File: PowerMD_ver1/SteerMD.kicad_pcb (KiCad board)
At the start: 2 copper layers, 75 x 88 mm, 216 parts, among them P1 SWD, P10 OUT_1, P11 ENC_0, P13 ENC_1, P14 I/O_1, P15 OUT_0, P2 MOTOR_COOLING, P3 CAN, P4 CAN, P5 SERIAL, P6 I/O_0, P7 FAN, P8 BATT_IN, P9 BATT_IN, Q1 MOSFET_N, Q2 MOSFET_N, Q3 MOSFET_N, Q4 MOSFET_N, Q5 MOSFET_N, Q6 MOSFET_N, Q7 MOSFET_N, Q8 MOSFET_N, SW1 RST, SW3 SW0, SW4 SW1, U1 MAX3051, U10 ACS758, U11 POWER_ON, U12 SI8274, U13 ACS758, U14 SI8274, U15 AZ1086H, U16 LOGO, U17 AQM0802, U19 ADRESS, U2 BD9G101, U3 STM32F405RG, U4 SI8274, U5 SI8900, U6 ADC_~RST, U7 BD9G101G, U8 SI8274, U9 BD33FA1, Y1 8MHz

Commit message: ハイサイド電流センシングバージョンとローサイド電流センシングバージョン
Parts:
- moved C34 0.55 mm to (82.2, 83.4)
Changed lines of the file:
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@@
   )
   (setup
-    (last_trace_width 0.25)
+    (last_trace_width 0.2)
     (user_trace_width 0.2)
     (user_trace_width 0.3)
@@
   )
   (module Mizz_lib:C_Radial_D13.0mm_H25.0mm_P5.00mm (layer F.Cu)
-    (at 82.25 83.975 180)
+    (at 82.22 83.43 180)
     (descr "C, Radial series, Radial, pin pitch=5.00mm, diameter=12.5mm, height=25mm, Non-Polar Electrolytic Capacitor")
     (tags "C Radial series Radial pin pitch 5.00mm diameter 12.5mm height 25mm Non-Polar Electrolytic Capacitor")
@@
   (via (at 110.87 118.57) (size 0.5) (drill 0.3) (layers F.Cu B.Cu) (net 2))
   (via (at 103.6 117.3) (size 0.8) (drill 0.4) (layers F.Cu B.Cu) (net 2))
-  (via (at 96.45 110) (size 0.5) (drill 0.3) (layers F.Cu B.Cu) (net 2))
   (via (at 102.35 110) (size 0.5) (drill 0.3) (layers F.Cu B.Cu) (net 2))
   (via (at 101.6 108.35) (size 0.5) (drill 0.3) (layers F.Cu B.Cu) (net 2))
@@
   (via (at 120.95 123.3) (size 0.5) (drill 0.3) (layers F.Cu B.Cu) (net 2))
   (via (at 79.05 113.15) (size 0.8) (drill 0.4) (layers F.Cu B.Cu) (net 2))
+  (via (at 96.45 110) (size 0.5) (drill 0.3) (layers F.Cu B.Cu) (net 2) (status 1000000))
   (segment (start 139.95 129.3375) (end 140.5125 129.9) (width 0.25) (layer B.Cu) (net 3))
   (segment (start 139.95 126.7) (end 139.95 129.3375) (width 0.25) (layer B.Cu) (net 3))
@@
   (segment (start 112.746179 113.653159) (end 112.687979 113.653159) (width 0.2) (layer F.Cu) (net 69))
   (segment (start 112.687979 113.653159) (end 111.864589 112.829769) (width 0.2) (layer F.Cu) (net 69))
+  (segment (start 106.80001 109.40001) (end 110.775001 113.375001) (width 0.25) (layer B.Cu) (net 69))
   (segment (start 90.68 112.2) (end 92.3 112.2) (width 0.25) (layer B.Cu) (net 69))
-  (segment (start 111.319357 113.375001) (end 111.864589 112.829769) (width 0.25) (layer B.Cu) (net 69))
   (segment (start 90.225 112.655) (end 90.68 112.2) (width 0.25) (layer B.Cu) (net 69))
-  (segment (start 92.3 112.2) (end 95.09999 109.40001) (width 0.25) (layer B.Cu) (net 69))
   (segment (start 95.09999 109.40001) (end 106.80001 109.40001) (width 0.25) (layer B.Cu) (net 69))
-  (segment (start 106.80001 109.40001) (end 110.775001 113.375001) (width 0.25) (layer B.Cu) (net 69))
+  (segment (start 111.319357 113.375001) (end 111.864589 112.829769) (width 0.25) (layer B.Cu) (net 69))
+  (segment (start 92.3 112.2) (end 95.09999 109.40001) (width 0.25) (layer B.Cu) (net 69))
   (segment (start 110.775001 113.375001) (end 111.319357 113.375001) (width 0.25) (layer B.Cu) (net 69))
   (via (at 111.05 112.8) (size 0.5) (drill 0.3) (layers F.Cu B.Cu) (net 70))
@@
   (segment (start 108.174999 109.924999) (end 111.05 112.8) (width 0.25) (layer B.Cu) (net 70))
   (segment (start 107.2 108.95) (end 108.174999 109.924999) (width 0.25) (layer B.Cu) (net 70))
-  (segment (start 90.685 108.845) (end 91.296494 109.456494) (width 0.25) (layer B.Cu) (net 70))
+  (segment (start 90.685 108.845) (end 91.296494 109.456494) (width 0.25) (layer B.Cu) (net 70) (status 1000000))
+  (segment (start 93.93858 109.92501) (end 94.91359 108.95) (width 0.25) (layer B.Cu) (net 70) (status 1000000))
+  (segment (start 90.225 108.845) (end 90.685 108.845) (width 0.25) (layer B.Cu) (net 70) (status 1000000))
+  (segment (start 91.3 109.456494) (end 91.768516 109.92501) (width 0.25) (layer B.Cu) (net 70) (status 1000000))
+  (segment (start 91.296494 109.456494) (end 91.3 109.456494) (width 0.25) (layer B.Cu) (net 70) (status 1000000))
+  (segment (start 91.768516 109.92501) (end 93.93858 109.92501) (width 0.25) (layer B.Cu) (net 70) (status 1000000))
   (segment (start 94.91359 108.95) (end 107.2 108.95) (width 0.25) (layer B.Cu) (net 70))
-  (segment (start 91.3 109.456494) (end 91.768516 109.92501) (width 0.25) (layer B.Cu) (net 70))
-  (segment (start 91.296494 109.456494) (end 91.3 109.456494) (width 0.25) (layer B.Cu) (net 70))
-  (segment (start 91.768516 109.92501) (end 93.93858 109.92501) (width 0.25) (layer B.Cu) (net 70))
-  (segment (start 90.225 108.845) (end 90.685 108.845) (width 0.25) (layer B.Cu) (net 70))
-  (segment (start 93.93858 109.92501) (end 94.91359 108.95) (width 0.25) (layer B.Cu) (net 70))
   (segment (start 140.885 105.725) (end 140.885 104.6) (width 0.2) (layer F.Cu) (net 71))
   (segment (start 121.832501 111.527499) (end 123.89 109.47) (width 0.2) (layer F.Cu) (net 71))
@@
   (segment (start 109.1 107.4) (end 105.95501 110.54499) (width 0.2) (layer F.Cu) (net 109))
   (segment (start 105.95501 110.54499) (end 94.95501 110.54499) (width 0.2) (layer F.Cu) (net 109))
-  (segment (start 112.59 107.4) (end 109.1 107.4) (width 0.2) (layer F.Cu) (net 109))
   (segment (start 94.95501 110.54499) (end 94.35001 111.14999) (width 0.2) (layer F.Cu) (net 109))
   (segment (start 94.35001 111.14999) (end 94.35001 118.55001) (width 0.2) (layer F.Cu) (net 109))
   (segment (start 94.35001 118.55001) (end 94.599989 118.799989) (width 0.2) (layer F.Cu) (net 109))
-  (segment (start 97.412501 119.199999) (end 97.9625 118.65) (width 0.2) (layer F.Cu) (net 110))
-  (segment (start 94.299999 119.199999) (end 97.412501 119.199999) (width 0.2) (layer F.Cu) (net 110))
-  (segment (start 93.95 118.85) (end 94.299999 119.199999) (width 0.2) (layer F.Cu) (net 110))
-  (segment (start 93.95 110.95) (end 93.95 118.85) (width 0.2) (layer F.Cu) (net 110))
-  (segment (start 94.9 110) (end 93.95 110.95) (width 0.2) (layer F.Cu) (net 110))
-  (segment (start 94.9 110) (end 95.6 110) (width 0.2) (layer F.Cu) (net 110))
-  (segment (start 95.6 110) (end 97.1 108.5) (width 0.2) (layer F.Cu) (net 110))
-  (segment (start 97.1 108.5) (end 97.1 106.6) (width 0.2) (layer F.Cu) (net 110))
+  (segment (start 112.59 107.4) (end 109.1 107.4) (width 0.2) (layer F.Cu) (net 109))
   (segment (start 96.595 106.095) (end 97.1 106.6) (width 0.2) (layer F.Cu) (net 110))
+  (segment (start 93.95 110.95) (end 93.95 118.85) (width 0.2) (layer F.Cu) (net 110))
   (segment (start 93.395 106.095) (end 96.595 106.095) (width 0.2) (layer F.Cu) (net 110))
   (segment (start 92.09 107.4) (end 93.395 106.095) (width 0.2) (layer F.Cu) (net 110))
+  (segment (start 95.6 110) (end 97.1 108.5) (width 0.2) (layer F.Cu) (net 110))
+  (segment (start 94.9 110) (end 95.6 110) (width 0.2) (layer F.Cu) (net 110))
+  (segment (start 97.1 108.5) (end 97.1 106.6) (width 0.2) (layer F.Cu) (net 110))
+  (segment (start 94.9 110) (end 93.95 110.95) (width 0.2) (layer F.Cu) (net 110))
+  (segment (start 97.412501 119.199999) (end 97.9625 118.65) (width 0.2) (layer F.Cu) (net 110))
+  (segment (start 93.95 118.85) (end 94.299999 119.199999) (width 0.2) (layer F.Cu) (net 110))
+  (segment (start 94.299999 119.199999) (end 97.412501 119.199999) (width 0.2) (layer F.Cu) (net 110))
   (segment (start 111.005 95.18) (end 110.9 95.075) (width 0.5) (layer F.Cu) (net 119))
   (segment (start 111.005 97.675) (end 111.005 95.18) (width 0.5) (layer F.Cu) (net 119))

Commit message: 途中
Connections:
- C20 pad 2: GNDPWR -> /MOTOR0_BATT
- C31 pad 2: GNDPWR -> /MOTOR0_BATT
- C46 pad 2: GNDPWR -> /MOTOR1_BATT
- C49 pad 2: GNDPWR -> /MOTOR1_BATT
- Q1 pad D: /MOTOR0_BATT -> +BATT
- Q2 pad S: GNDPWR -> /MOTOR0_BATT
- Q3 pad D: /MOTOR1_BATT -> +BATT
- Q4 pad S: GNDPWR -> /MOTOR1_BATT
- Q5 pad D: /MOTOR0_BATT -> +BATT
- Q6 pad S: GNDPWR -> /MOTOR0_BATT
- Q7 pad D: /MOTOR1_BATT -> +BATT
- Q8 pad S: GNDPWR -> /MOTOR1_BATT
- U10 pad 4: +BATT -> /MOTOR0_BATT
- U10 pad 5: /MOTOR0_BATT -> GNDPWR
- U12 pad 9: GNDPWR -> /MOTOR0_BATT
- U13 pad 4: +BATT -> /MOTOR1_BATT
- U13 pad 5: /MOTOR1_BATT -> GNDPWR
- U14 pad 9: GNDPWR -> /MOTOR1_BATT
- U4 pad 9: GNDPWR -> /MOTOR0_BATT
- U8 pad 9: GNDPWR -> /MOTOR1_BATT
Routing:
- net GNDPWR: track 77.2 -> 66.6 mm, vias 36 -> 32
- net /MOTOR1_BATT: track 0.00 -> 5.31 mm, vias 38 -> 2
- net +BATT: track 104.8 -> 108.9 mm
- net /MOTOR0_BATT: track 4.09 -> 5.31 mm, vias 35 -> 2
- net +12P: track 89.4 -> 89.9 mm
- removed copper zone on B.Cu, net +BATT
- removed copper zone on F.Cu, net /MOTOR0_BATT
- removed copper zone on F.Cu, net /MOTOR1_BATT
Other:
- board text added: "CAN DC-MotroDriver Aqualius Sadalmeric ver.1.0"
- board text removed: "CAN DC-MotroDriver Aqualius Sadalmeric ver.0.0"

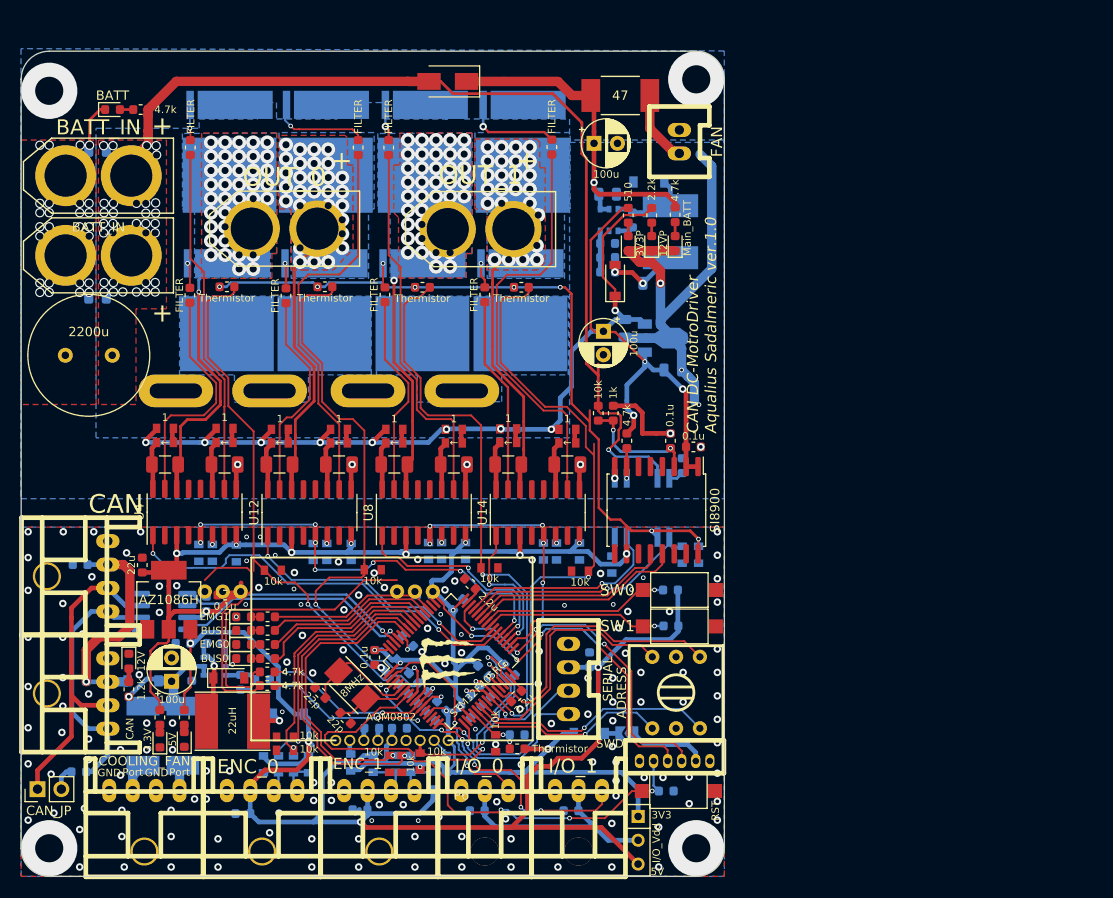
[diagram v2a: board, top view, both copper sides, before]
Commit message: Power MD 電流センシングをローサイドでセンシングするように変更した&DAC乗っけた
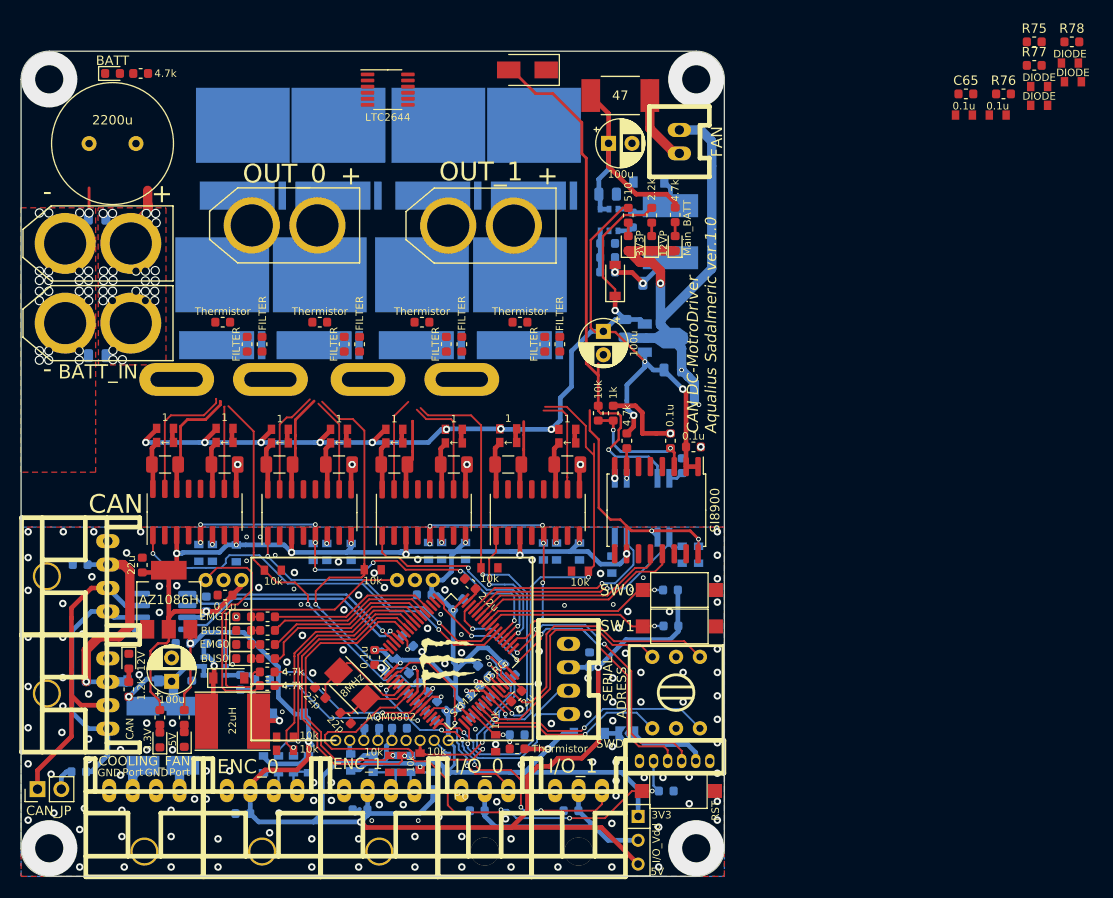
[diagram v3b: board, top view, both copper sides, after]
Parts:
- added C27: 0.1u, Mizz_lib:1608_WP, F.Cu at (173.1, 57.8)
- added C51: 0.1u, Mizz_lib:1608_WP, F.Cu at (176.7, 57.8)
- added C65: 0.1u, Capacitor_SMD:C_0603_1608Metric, F.Cu at (173.3, 55.6)
- added D10: DIODE, Mizz_lib:1608_WP, F.Cu at (184.3, 52.3)
- added D12: DIODE, Mizz_lib:1608_WP, F.Cu at (181.1, 56.8)
- added D17: DIODE, Mizz_lib:1608_WP, F.Cu at (184.7, 54.3)
- added D6: DIODE, Mizz_lib:1608_WP, F.Cu at (181.1, 54.8)
- added R75: 10k, Resistor_SMD:R_0603_1608Metric, F.Cu at (180.5, 50.0)
- added R76: 1k, Resistor_SMD:R_0603_1608Metric, F.Cu at (177.3, 55.6)
- added R77: 10k, Resistor_SMD:R_0603_1608Metric, F.Cu at (180.5, 52.5)
- added R78: 1k, Resistor_SMD:R_0603_1608Metric, F.Cu at (184.6, 50.0)
- added U18: LTC2644, Package_SO:MSOP-12_3x4mm_P0.65mm, F.Cu at (111.6, 55.1)
- moved C34 22.7 mm to (84.8, 60.9)
- moved R54 22.4 mm to (119.5, 82.2)
- moved R18 22.3 mm to (98.2, 82.2)
- moved R64 21.0 mm to (129.9, 82.2)
- moved R31 21.0 mm to (108.6, 82.2)
- moved Q1 17.3 mm to (96.2, 61.4), turned to 180 degrees
- moved Q3 17.3 mm to (117.0, 61.4), turned to 180 degrees
- moved Q5 17.3 mm to (106.3, 61.4), turned to 180 degrees
- moved Q7 17.3 mm to (127.2, 61.4), turned to 180 degrees
- moved Q2 15.6 mm to (94.0, 77.3), turned to 180 degrees
- moved Q6 15.6 mm to (104.3, 77.3), turned to 180 degrees
- moved Q4 15.6 mm to (115.2, 77.3), turned to 180 degrees
- moved Q8 15.6 mm to (125.7, 77.3), turned to 180 degrees
- moved D15 8.59 mm to (126.5, 53.0)
- moved R53 8.41 mm to (117.8, 82.2)
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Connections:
- U5 pad 4: /CounterVoltage0 -> /MOTOR0_VOLTAGE_DAC
- U5 pad 5: /CounterVoltage1 -> /MOTOR1_VOLTAGE_DAC
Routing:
- net +3V3: track 289.3 -> 236.2 mm, vias 25 -> 20
- net +BATT: track 108.9 -> 65.0 mm, vias 34 -> 27
- net Net-(R64-Pad2): track 44.4 -> 10.6 mm
- net Net-(R31-Pad2): track 42.0 -> 10.0 mm
- net Net-(R54-Pad2): track 40.0 -> 11.6 mm
- net Net-(R18-Pad2): track 37.1 -> 8.79 mm
- net /OUT1_R: track 30.2 -> 7.39 mm, vias 25 -> 0
- net Net-(R63-Pad2): track 20.9 -> 0.00 mm
- net /OUT0_R: track 30.8 -> 10.4 mm, vias 29 -> 0
- net /OUT1_L: track 27.7 -> 7.50 mm, vias 38 -> 0
- net /OUT0_L: track 31.4 -> 13.9 mm, vias 38 -> 0
- net /Motor1R_Tmp: track 69.8 -> 52.6 mm
- net /Motor0L_Tmp: track 62.6 -> 45.5 mm
- net /Motor0R_Tmp: track 63.2 -> 47.3 mm
- net /Motor1L_Tmp: track 65.8 -> 50.5 mm
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- removed copper zone on B.Cu, net /MOTOR0_BATT
- removed copper zone on B.Cu, net /MOTOR1_BATT
- removed copper zone on B.Cu, net /OUT0_L
- removed copper zone on F.Cu, net /OUT0_L
- removed copper zone on B.Cu, net /OUT0_R
- removed copper zone on F.Cu, net /OUT0_R
- removed copper zone on B.Cu, net /OUT1_L
- removed copper zone on F.Cu, net /OUT1_L
- removed copper zone on B.Cu, net /OUT1_R
- removed copper zone on F.Cu, net /OUT1_R
- removed copper zone on B.Cu, net GNDPWR
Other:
- board text added: "-"

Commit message: ブラシレス復元の続き
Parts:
- R17, R18, R30, R31, R53, R54, R63, R64: footprint Resistor_SMD:R_0603_1608Metric -> Mizz_lib:1608_WP
- TH1, TH2, TH3, TH4: footprint Capacitor_SMD:C_0603_1608Metric -> Mizz_lib:1608_WP
- moved TH1 0.65 mm to (93.3, 79.9)
- moved TH4 0.60 mm to (125.1, 79.9)
- moved TH2 0.60 mm to (114.7, 79.9)
- moved TH3 0.60 mm to (103.8, 79.9)

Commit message: だいぶ良いところまで進んだ
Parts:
- added C66: 0.1u, Mizz_lib:1608_WP, F.Cu at (115.3, 58.5)
- added C67: 0.1u, Mizz_lib:1608_WP, F.Cu at (107.0, 58.5)
- C65: footprint Capacitor_SMD:C_0603_1608Metric -> Mizz_lib:1608_WP
- D1, D10, D11, D12, D13, D14, D17, D19, D2, D20, D3, D6: footprint Mizz_lib:1608_WP -> Diode_SMD:D_SOD-123
- R19, R20, R28, R29, R55, R56, R58, R59: value 1 -> 10
- R40: value 4.7k -> 20k
- R75, R76, R77, R78: footprint Resistor_SMD:R_0603_1608Metric -> Mizz_lib:1608_WP
- moved D17 81.9 mm to (102.8, 55.9), turned to 180 degrees
- moved R78 79.2 mm to (105.8, 58.5), turned to 270 degrees
- moved D12 78.4 mm to (102.8, 53.6), turned to 180 degrees
- moved R77 76.4 mm to (104.4, 58.5), turned to 90 degrees
- moved D10 66.2 mm to (118.2, 53.7)
- moved C27 64.7 mm to (108.5, 60.5), turned to 180 degrees
- moved C51 64.4 mm to (112.3, 60.5)
- moved R75 64.4 mm to (116.8, 58.5), turned to 90 degrees
- moved R76 63.4 mm to (114.0, 58.5), turned to 270 degrees
- moved D6 62.9 mm to (118.2, 56.0)
- moved C65 59.3 mm to (114.0, 55.4), turned to 90 degrees
- moved P15 1.86 mm to (99.5, 68.1)
- moved U18 1.71 mm to (111.0, 56.7), turned to 90 degrees
- moved P10 1.70 mm to (120.8, 68.1)
- moved Q1 1.51 mm to (95.3, 60.1)
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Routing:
- net +12P: track 89.9 -> 21.8 mm, vias 9 -> 1
- net /MOTOR0_VOLTAGE_DAC: track 0.00 -> 63.7 mm, vias 0 -> 2
- net /MOTOR1_VOLTAGE_DAC: track 0.00 -> 62.4 mm, vias 0 -> 2
- net +BATT: track 65.0 -> 118.3 mm, vias 27 -> 26
- net GNDPWR: track 69.3 -> 86.2 mm, vias 30 -> 29
- net +3.3VP: track 47.5 -> 63.5 mm
- net /OUT1_R: track 7.39 -> 18.9 mm, vias 0 -> 1
- net /MOTOR0_OUT: track 0.00 -> 11.1 mm
- net /MOTOR1_OUT: track 0.00 -> 10.8 mm
- net /OUT0_L: track 13.9 -> 4.20 mm
- net /Motor1R_Tmp: track 52.6 -> 43.9 mm
- net /OUT0_R: track 10.4 -> 2.64 mm
- net /OUT1_L: track 7.50 -> 14.7 mm, vias 0 -> 1
- net Net-(D10-Pad1): track 0.00 -> 6.73 mm
- net Net-(D12-Pad1): track 0.00 -> 6.65 mm
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- added copper zone on B.Cu, net +BATT
- added copper zone on B.Cu, net /MOTOR0_BATT
- added copper zone on B.Cu, net /MOTOR1_BATT
- added copper zone on B.Cu, net /OUT0_L
- added copper zone on B.Cu, net /OUT0_R
- added copper zone on B.Cu, net /OUT1_L
- added copper zone on B.Cu, net /OUT1_R
- added copper zone on B.Cu, net GNDPWR
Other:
- board text added: "Designed by A.Mizuta in 2020/02/22."
- board text removed: "Designed by A.Mizuta in 2020/01/07."
